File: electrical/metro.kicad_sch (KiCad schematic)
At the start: 44 parts, among them Q1 AO3401A, Q2 AO3400A, SW1 SW_Push, SW2 SW_Push, SW3 SW_Push, U1 ATTINY1616-MN, U2 MCP73831-2-OT, U3 XC6206PxxxMR, Y1 32.678

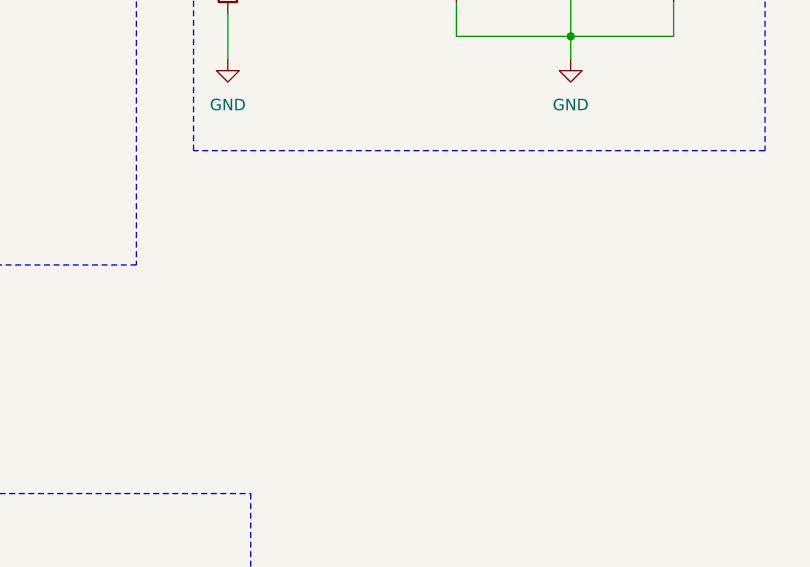
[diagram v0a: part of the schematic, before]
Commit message: Basic vibration with breakout board
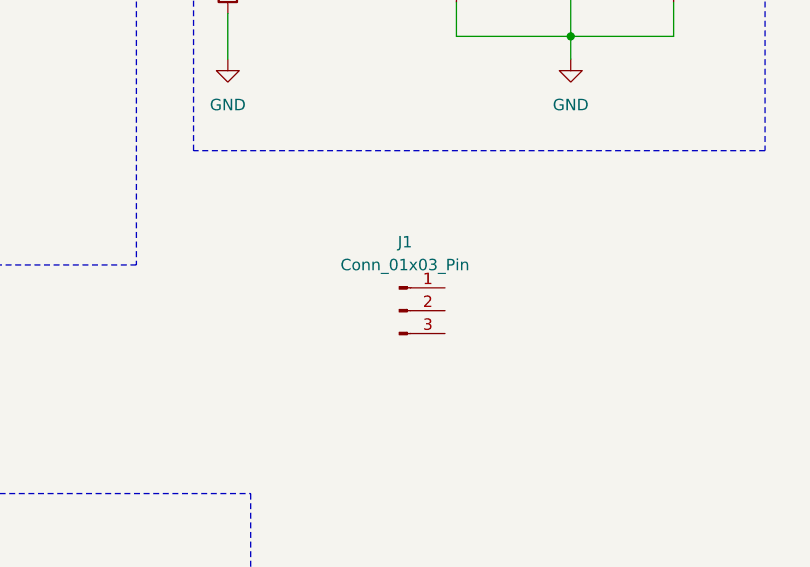
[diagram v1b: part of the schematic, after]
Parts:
- added J1: Conn_01x03_Pin, Connector_PinHeader_2.54mm:PinHeader_1x03_P2.54mm_Vertical_SMD_Pin1Left, symbol Connector:Conn_01x03_Pin
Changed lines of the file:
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@@
+	)
+	(symbol
+		(lib_id "Connector:Conn_01x03_Pin")
+		(at 143.51 93.98 0)
+		(unit 1)
+		(exclude_from_sim no)
+		(in_bom yes)
+		(on_board yes)
+		(dnp no)
+		(fields_autoplaced yes)
+		(property "Reference" "J1"
+			(at 144.145 86.36 0)
+			(effects
+				(font
+					(size 1.27 1.27)
+				)
+			)
+		)
+		(property "Value" "Conn_01x03_Pin"
+			(at 144.145 88.9 0)
+			(effects
+				(font
+					(size 1.27 1.27)
+				)
+			)
+		)
+		(property "Footprint" "Connector_PinHeader_2.54mm:PinHeader_1x03_P2.54mm_Vertical_SMD_Pin1Left"
+			(at 143.51 93.98 0)
+			(effects
+				(font
+					(size 1.27 1.27)
+				)
+				(hide yes)
+			)
+		)
+		(property "Datasheet" "~"
+			(at 143.51 93.98 0)
+			(effects
+				(font
+					(size 1.27 1.27)
+				)
+				(hide yes)
+			)
+		)
+		(property "Description" "Generic connector, single row, 01x03, script generated"
+			(at 143.51 93.98 0)
+			(effects
+				(font
+					(size 1.27 1.27)
+				)
+				(hide yes)
+			)
+		)
+		(pin "3"
+		)
+		(pin "2"
+		)
+		(pin "1"
+		)
+		(instances
+			(project ""
+				(path "/b3f6d6fe-a5b4-421c-a9bd-ce203989d1c4"
+					(reference "J1")
+					(unit 1)
+				)
+			)
+		)
 	)
 	(symbol

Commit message: Circuit mostly complete with driver
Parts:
- removed +MOTOR1, +VBAT1: ~, TestPoint:TestPoint_THTPad_1.5x1.5mm_Drill0.7mm, symbol Connector:TestPoint
- removed -MOTOR1, -VBAT1: ~, TestPoint:TestPoint_THTPad_D1.5mm_Drill0.7mm, symbol Connector:TestPoint
- removed C3: 20pF, Capacitor_SMD:C_0402_1005Metric, symbol Device:C
- removed C8: 100nF, Capacitor_SMD:C_0402_1005Metric, symbol Device:C
- removed C9: 10μF, Capacitor_SMD:C_0402_1005Metric, symbol Device:C
- removed D9: D_Schottky, Diode_SMD:D_SOD-123, symbol Device:D_Schottky
- removed J1: Conn_01x03_Pin, Connector_PinHeader_2.54mm:PinHeader_1x03_P2.54mm_Vertical_SMD_Pin1Left, symbol Connector:Conn_01x03_Pin
- removed Q2: AO3400A, Package_TO_SOT_SMD:SOT-23, symbol Transistor_FET:AO3400A
- removed Y1: 32.678, Crystal:Crystal_SMD_3215-2Pin_3.2x1.5mm, symbol Device:Crystal
- added C5: 10μF, Capacitor_SMD:C_0402_1005Metric, symbol Device:C
- added C6: 1μF, Capacitor_SMD:C_0402_1005Metric, symbol Device:C
- added D1: Blue, LED_SMD:LED_0402_1005Metric, symbol Device:LED
- added FID1, FID2, FID3: Fiducial, Fiducial:Fiducial_0.5mm_Mask1mm, symbol Mechanical:Fiducial
- added J1, J2, J4: Conn_01x02, Connector_Wire:SolderWire-0.15sqmm_1x02_P4mm_D0.5mm_OD1.5mm, symbol Connector_Generic:Conn_01x02
- added J3: Conn_01x03, Connector_Wire:SolderWire-0.1sqmm_1x03_P3.6mm_D0.4mm_OD1mm, symbol Connector_Generic:Conn_01x03
- added R1: 2k2, Capacitor_SMD:C_0402_1005Metric, symbol Device:R
- added U3: DRV2605LDGS, Package_SO:VSSOP-10_3x3mm_P0.5mm, symbol Driver_Haptic:DRV2605LDGS
- C4: value 20pF -> 1μF
- D9: renamed from D8; LCSC PN (none) -> C8598
- Q1: LCSC PN (none) -> C20917
- R10: value 100kR -> 4k7
- R11: value 100R -> 4k7
- R2: renamed from R1; value 680R -> 2k2
- R3: renamed from R2; value 680R -> 2k2
- R4: renamed from R3; value 680R -> 2k2
- R5: renamed from R4; value 680R -> 2k2
- R6: renamed from R5; value 680R -> 2k2
- R7: renamed from R6; value 10kR -> 33k
- R8: renamed from R7; value 680R -> 2k2
- R9: renamed from R8; value 680R -> 10k
- SW1: renamed from SW3; LCSC PN (none) -> C720477
- SW2: LCSC PN (none) -> C720477
- SW3: renamed from SW1; LCSC PN (none) -> C720477
- U1: renamed from U2; value MCP73831-2-OT -> MCP73831T-2ACI/OT; LCSC PN (none) -> C424093
- U2: renamed from U1; LCSC PN (none) -> C507118
- U4: renamed from U3; value XC6206PxxxMR -> XC6206P332MR-G; LCSC PN (none) -> C5446
- renumbered C5 to C1, C1 to C2, C2 to C3, C6 to C8, D1 to D2, D2 to D3, D3 to D4, D4 to D5, D5 to D6, D6 to D7, D7 to D8, R9 to R12
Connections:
- net +3V3: now also C4.1, R10.2, R11.2, C5.1, J3.2 (Pin_2), R1.1, U3.10 (VDD), U3.5 (EN), U3.6 (VDD/NC)
- net GND: now also SW1.2, SW2.2, SW3.2, C5.2, C6.2, J1.2 (Pin_2), J2.2 (Pin_2), J3.3 (Pin_3), U3.4 (IN/TRIG), U3.8 (GND); no longer R10.1, SW1.1, SW2.1, SW3.1
- net LED1: now also U2.6 (PA5); no longer U2.5 (PA4)
- net SW1: now reaches U2.1 (PA2)
- net SW1: now also SW1.1
- net at U2.11 (PB3/TOSC1): no longer C4.1
- net SW2: now reaches U2.12 (PB2/TOSC2)
- net SW2: now also SW2.1
- net SDA: now reaches U2.13 (PB1)
- net SDA: now also R11.1, U3.2 (SCL)
- net SCL: now reaches U2.14 (PB0)
- net SCL: now also R10.1, U3.3 (SDA)
- net STATUS: now reaches U2.15 (PC0)
- net STATUS: now also D1.1 (K)
- net at U2.16 (PC1): no longer SW3.2
- net SW3: now reaches U2.17 (PC2)
- net SW3: now also SW3.1; no longer SW2.2
- net at U2.18 (PC3): no longer SW1.2
- net LIPO STAT: now reaches R8.1, R9.1, U1.1 (STAT)
- net +5V renamed +VBUS
- net +VBUS: now also J1.1 (Pin_1)
- net +VBAT renamed +BATT
- net +BATT: now also J2.1 (Pin_1)
- removed net MOTOR: R10.2, R11.2, U2.6 (PA5)
- net UDPI renamed UPDI
- net UPDI: now also J3.1 (Pin_1)
- new net: D1.2 (A), R1.2
- new net: C6.1, U3.1 (REG)
- new net MOTOR+: J4.1 (Pin_1), U3.7 (OUT+)
- new net MOTOR-: J4.2 (Pin_2), U3.9 (OUT-)
- no-connect marks 0 -> 6
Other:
- company: Max Tarver Industries -> (none)
- title: Wearable Metronome -> Metro
- moved on the sheet: C1, C2, C3, C7, C8, D2, D3, D4, D5, D6, D7, D8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

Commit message: new led setup
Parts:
- removed D1: Blue, LED_SMD:LED_0402_1005Metric, symbol Device:LED
- removed D8: Green, LED_SMD:LED_0402_1005Metric, symbol Device:LED
- removed FID1, FID2, FID3: Fiducial, Fiducial:Fiducial_0.5mm_Mask1mm, symbol Mechanical:Fiducial
- removed H1, H2: M2, MountingHole:MountingHole_2.2mm_M2, symbol Mechanical:MountingHole
- removed J3: Conn_01x03, Connector_Wire:SolderWire-0.1sqmm_1x03_P3.6mm_D0.4mm_OD1mm, symbol Connector_Generic:Conn_01x03
- removed R1: 2k2, Capacitor_SMD:C_0402_1005Metric, symbol Device:R
- removed R9: 10k, Capacitor_SMD:C_0402_1005Metric, symbol Device:R
- removed SW1, SW2, SW3: SW_Push, TS-1088-AR02016:SW_TS-1088-AR02016, symbol TS-1088-AR02016:TS-1088-AR02016
- added S1, S2, S3: EVQ-P7C01P, EVQ-P7C01P:SW_EVQ-P7C01P, symbol EVQ-P7C01P:EVQ-P7C01P
- added TP1: UPDI, TestPoint:TestPoint_THTPad_D1.0mm_Drill0.5mm, symbol Connector:TestPoint
- D1: renamed from D2; footprint LED_SMD:LED_0402_1005Metric -> LTST-C230KRKT:LED_LTST-C230KRKT; symbol Device:LED -> LTST-C230KRKT:LTST-C230KRKT; LCSC PN (none) -> C125107
- D2: renamed from D3; footprint LED_SMD:LED_0402_1005Metric -> LTST-C230KRKT:LED_LTST-C230KRKT; symbol Device:LED -> LTST-C230KRKT:LTST-C230KRKT; LCSC PN (none) -> C125107
- D3: renamed from D4; footprint LED_SMD:LED_0402_1005Metric -> LTST-C230KRKT:LED_LTST-C230KRKT; symbol Device:LED -> LTST-C230KRKT:LTST-C230KRKT; LCSC PN (none) -> C125107
- D4: renamed from D5; footprint LED_SMD:LED_0402_1005Metric -> LTST-C230KRKT:LED_LTST-C230KRKT; symbol Device:LED -> LTST-C230KRKT:LTST-C230KRKT; LCSC PN (none) -> C125107
- D5: renamed from D6; footprint LED_SMD:LED_0402_1005Metric -> LTST-C230KRKT:LED_LTST-C230KRKT; symbol Device:LED -> LTST-C230KRKT:LTST-C230KRKT; LCSC PN (none) -> C125107
- D6: renamed from D7; footprint LED_SMD:LED_0402_1005Metric -> LTST-C230KRKT:LED_LTST-C230KRKT; symbol Device:LED -> LTST-C230KRKT:LTST-C230KRKT; LCSC PN (none) -> C125107
- D7: renamed from D9; value D_Schottky -> 1N5819WS; footprint Diode_SMD:D_SOD-123 -> Diode_SMD:D_SOD-323; LCSC PN C8598 -> C191023
- J1: renamed from J2; footprint Connector_Wire:SolderWire-0.15sqmm_1x02_P4mm_D0.5mm_OD1.5mm -> Connector_Wire:SolderWire-0.1sqmm_1x02_P3.6mm_D0.4mm_OD1mm
- J2: renamed from J1; footprint Connector_Wire:SolderWire-0.15sqmm_1x02_P4mm_D0.5mm_OD1.5mm -> Connector_Wire:SolderWire-0.1sqmm_1x02_P3.6mm_D0.4mm_OD1mm
- J3: renamed from J4; footprint Connector_Wire:SolderWire-0.15sqmm_1x02_P4mm_D0.5mm_OD1.5mm -> Connector_Wire:SolderWire-0.1sqmm_1x02_P3.6mm_D0.4mm_OD1mm
- R1: renamed from R2; footprint Capacitor_SMD:C_0402_1005Metric -> Resistor_SMD:R_0402_1005Metric
- R10: renamed from R12; footprint Capacitor_SMD:C_0402_1005Metric -> Resistor_SMD:R_0402_1005Metric
- R2: renamed from R3; footprint Capacitor_SMD:C_0402_1005Metric -> Resistor_SMD:R_0402_1005Metric
- R3: renamed from R4; footprint Capacitor_SMD:C_0402_1005Metric -> Resistor_SMD:R_0402_1005Metric
- R4: renamed from R5; footprint Capacitor_SMD:C_0402_1005Metric -> Resistor_SMD:R_0402_1005Metric
- R5: renamed from R6; footprint Capacitor_SMD:C_0402_1005Metric -> Resistor_SMD:R_0402_1005Metric
- R6: renamed from R7; footprint Capacitor_SMD:C_0402_1005Metric -> Resistor_SMD:R_0402_1005Metric
- R7: renamed from R8; footprint Capacitor_SMD:C_0402_1005Metric -> Resistor_SMD:R_0402_1005Metric
- R8: renamed from R10; footprint Capacitor_SMD:C_0402_1005Metric -> Resistor_SMD:R_0402_1005Metric
- R9: renamed from R11; footprint Capacitor_SMD:C_0402_1005Metric -> Resistor_SMD:R_0402_1005Metric
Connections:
- net +VBUS: now also D6.A; no longer D6.2 (A)
- net GND: now also S1.2_1, S1.2_2, S2.2_1, S2.2_2, S3.2_1, S3.2_2
- net LED1: now also D1.C, U2.10 (PB4); no longer D1.1 (K), U2.6 (PA5)
- net LED2: now also D2.C, U2.9 (PB5); no longer D2.1 (K), U2.7 (PA6)
- net LED3: now also D3.C; no longer D3.1 (K)
- net LED4: now also D4.C, U2.7 (PA6); no longer D4.1 (K), U2.9 (PB5)
- net LED5: now also D5.C, U2.6 (PA5); no longer D5.1 (K), U2.10 (PB4)
- net SW1: now also U2.17 (PC2), S1.1_1, S1.1_2; no longer U2.1 (PA2)
- net SW2: now also S2.1_1, S2.1_2
- net SW3: now also U2.1 (PA2), S3.1_1, S3.1_2; no longer U2.17 (PC2)
- net UPDI: now also TP1.1
- net at R1.2: now also D1.A; no longer D1.2 (A)
- net REG IN: now reaches C7.1, D7.1 (K), Q1.2 (S), U4.3 (VI)
- net at R3.2: now also D3.A; no longer D3.2 (A)
- net at R7.2: now also D6.C; no longer D6.1 (K)
- net at R4.2: now also D4.A; no longer D4.2 (A)
- net at R2.2: now also D2.A; no longer D2.2 (A)
- net at R5.2: now also D5.A; no longer D5.2 (A)
- net STATUS: no longer names the net of U2.15 (PC0)
- no-connect marks 6 -> 7
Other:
- moved on the sheet: J1, J2, J3, R1, R2, R3, R4, R5, R7

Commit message: Routing done
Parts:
- removed TP1: UPDI, TestPoint:TestPoint_THTPad_D1.0mm_Drill0.5mm, symbol Connector:TestPoint
- added J4: Conn_01x03, Connector_Wire:SolderWire-0.1sqmm_1x03_P3.6mm_D0.4mm_OD1mm, symbol Connector_Generic:Conn_01x03
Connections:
- net +3V3: now also J4.2 (Pin_2)
- net +VBUS: now also R7.2; no longer D6.A
- net GND: now also J4.3 (Pin_3)
- net LIPO STAT: now also D6.C; no longer R7.1
- net SW2: now also U2.1 (PA2); no longer U2.12 (PB2/TOSC2)
- net SW3: now also U2.12 (PB2/TOSC2); no longer U2.1 (PA2)
- net UPDI: now also J4.1 (Pin_1)
- new net: D6.A, R7.1
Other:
- moved on the sheet: D6, J1, J2, J3, R7

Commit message: Improve led footprint
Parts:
- D1, D2, D3, D4, D5, D6: footprint LTST-C230KRKT:LED_LTST-C230KRKT -> LTST-C230KRKT:Custom LTST-C230KRKT; symbol LTST-C230KRKT:LTST-C230KRKT -> Device:LED
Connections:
- net +3V3: now also D1.2 (A), D2.2 (A), D3.2 (A), D4.2 (A), D5.2 (A); no longer R1.1, R2.1, R3.1, R4.1, R5.1
- net +VBUS: now also D6.2 (A); no longer R7.2
- net LED1: now also R1.2; no longer D1.C
- net LED2: now also R2.2; no longer D2.C
- net LED3: now also R3.2; no longer D3.C
- net LED4: now also R4.2; no longer D4.C
- net LED5: now also R5.2; no longer D5.C
- net LIPO STAT: now also R7.1; no longer D6.C
- new net: D1.1 (K), R1.1
- new net: D3.1 (K), R3.1
- new net: D6.1 (K), R7.2
- new net: D4.1 (K), R4.1
- new net: D2.1 (K), R2.1
- new net: D5.1 (K), R5.1
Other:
- moved on the sheet: R1, R2, R3, R4, R5, R7

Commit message: rev 2 board. larger components
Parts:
- removed C7, C8: 1μF, Capacitor_SMD:C_0402_1005Metric, symbol Device:C
- removed Q1: AO3401A, Package_TO_SOT_SMD:SOT-23, symbol Transistor_FET:AO3401A
- removed R10: 100kR, Resistor_SMD:R_0402_1005Metric, symbol Device:R
- removed U4: XC6206P332MR-G, Package_TO_SOT_SMD:SOT-23-3, symbol Regulator_Linear:XC6206PxxxMR
- added C1: 1μF, Capacitor_SMD:C_0603_1608Metric_Pad1.08x0.95mm_HandSolder, symbol Device:C
- C2: renamed from C3; footprint Capacitor_SMD:C_0402_1005Metric -> Capacitor_SMD:C_0603_1608Metric_Pad1.08x0.95mm_HandSolder
- C3: renamed from C2; footprint Capacitor_SMD:C_0402_1005Metric -> Capacitor_SMD:C_0603_1608Metric_Pad1.08x0.95mm_HandSolder
- C4, C5: footprint Capacitor_SMD:C_0402_1005Metric -> Capacitor_SMD:C_0603_1608Metric_Pad1.08x0.95mm_HandSolder
- C6: renamed from C1; footprint Capacitor_SMD:C_0402_1005Metric -> Capacitor_SMD:C_0603_1608Metric_Pad1.08x0.95mm_HandSolder
- C7: renamed from C6; footprint Capacitor_SMD:C_0402_1005Metric -> Capacitor_SMD:C_0603_1608Metric_Pad1.08x0.95mm_HandSolder
- D7: value 1N5819WS -> D_Schottky; footprint Diode_SMD:D_SOD-323 -> Diode_SMD:D_SMA; LCSC PN C191023 -> (none)
- J1, J2, J3: footprint Connector_Wire:SolderWire-0.1sqmm_1x02_P3.6mm_D0.4mm_OD1mm -> Connector_PinHeader_2.54mm:PinHeader_1x02_P2.54mm_Vertical; now not fitted
- J4: footprint Connector_Wire:SolderWire-0.1sqmm_1x03_P3.6mm_D0.4mm_OD1mm -> Connector_PinHeader_2.54mm:PinHeader_1x03_P2.54mm_Vertical; now not fitted
- R1, R2, R3, R4, R5: footprint Resistor_SMD:R_0402_1005Metric -> Resistor_SMD:R_0603_1608Metric_Pad0.98x0.95mm_HandSolder
- R6: renamed from R8; footprint Resistor_SMD:R_0402_1005Metric -> Resistor_SMD:R_0603_1608Metric_Pad0.98x0.95mm_HandSolder
- R7: renamed from R9; footprint Resistor_SMD:R_0402_1005Metric -> Resistor_SMD:R_0603_1608Metric_Pad0.98x0.95mm_HandSolder
- R8: renamed from R6; footprint Resistor_SMD:R_0402_1005Metric -> Resistor_SMD:R_0603_1608Metric_Pad0.98x0.95mm_HandSolder
- R9: renamed from R7; footprint Resistor_SMD:R_0402_1005Metric -> Resistor_SMD:R_0603_1608Metric_Pad0.98x0.95mm_HandSolder
- renumbered U2 to U1, U1 to U2
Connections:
- net REG IN is gone; now on net +BATT: D7.1 (K)
- net +BATT: now also C2.1, C4.1, C5.1, D1.2 (A), D2.2 (A), D3.2 (A), D4.2 (A), D5.2 (A), R6.2, R7.2, U1.4 (VDD), U3.10 (VDD), U3.5 (EN), U3.6 (VDD/NC), C1.1
- net +VBUS: no longer D7.2 (A)
- net GND: now also C1.2
- net SCL: now also R7.1, U3.2 (SCL); no longer R6.1, U3.3 (SDA)
- net SDA: now also R6.1, U3.3 (SDA); no longer R7.1, U3.2 (SCL)
- removed net +3V3: C2.1, C4.1, C5.1, D1.2 (A), D2.2 (A), D3.2 (A), D4.2 (A), D5.2 (A), J4.2 (Pin_2), R6.2, R7.2, U1.4 (VDD), U3.10 (VDD), U3.5 (EN), U3.6 (VDD/NC)
- new net: D7.2 (A), J4.2 (Pin_2)
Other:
- moved on the sheet: C3, C6, D6, R8, R9, U2
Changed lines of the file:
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@@
 		(title "Metro")
 		(date "2026-01-21")
-		(rev "1")
+		(rev "2")
 	)
